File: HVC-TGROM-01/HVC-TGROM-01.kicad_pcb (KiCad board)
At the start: 2 copper layers, 90.1 x 56.8 mm, 1 part

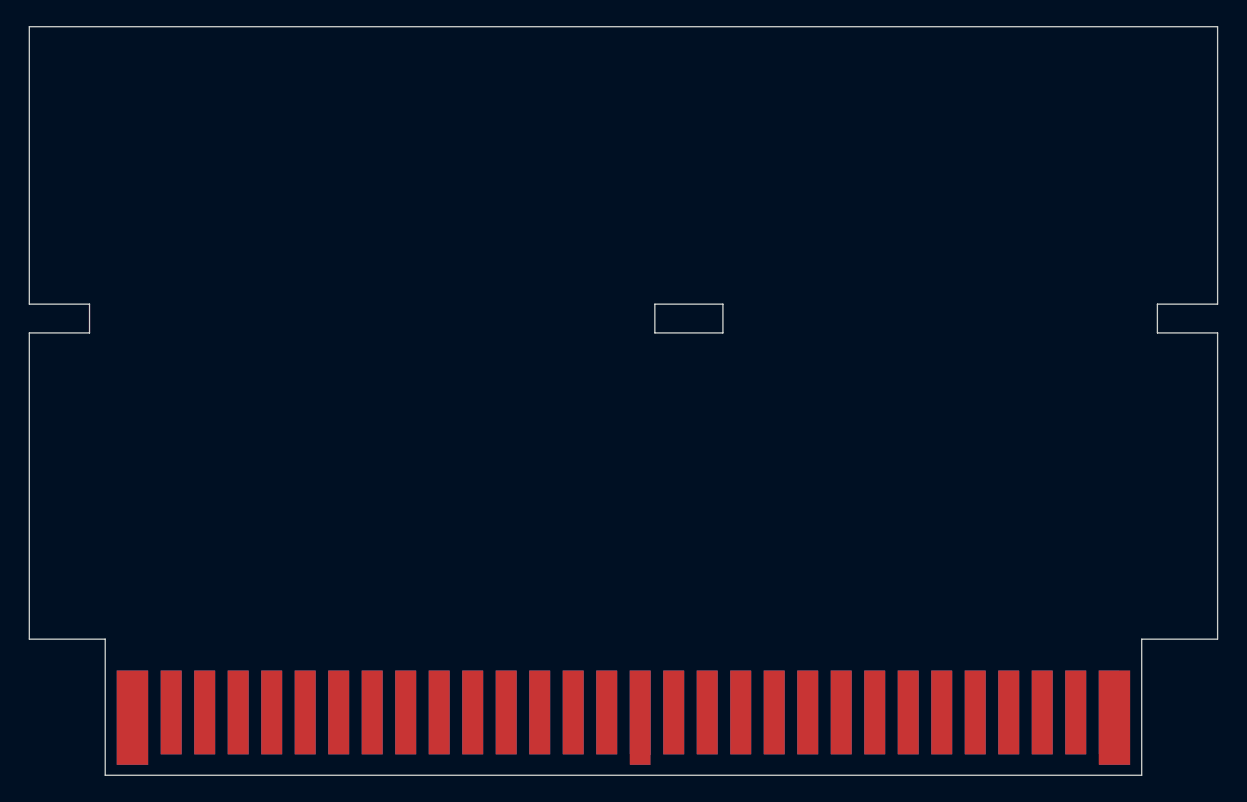
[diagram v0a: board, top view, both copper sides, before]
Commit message: update TxROM measurements
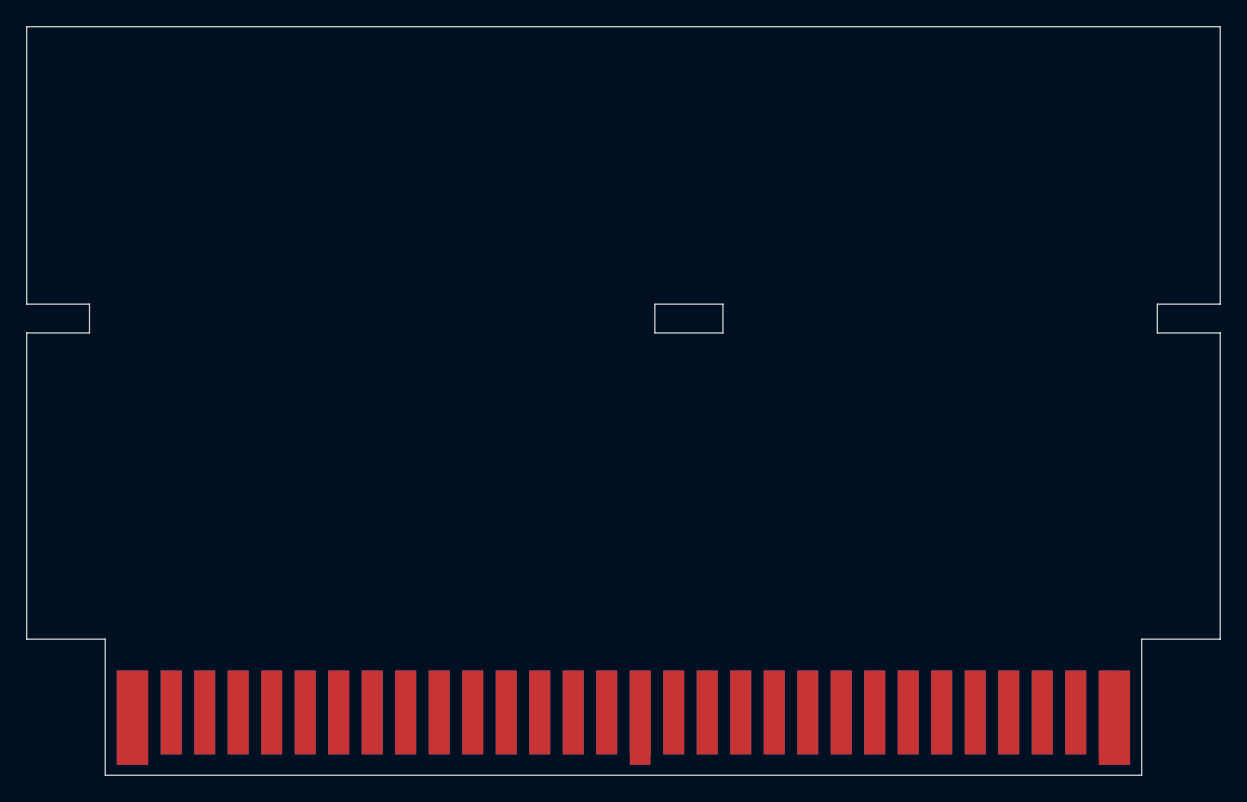
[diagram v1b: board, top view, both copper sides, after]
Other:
- board size 90.1 x 56.8 mm -> 90.5 x 56.8 mm
